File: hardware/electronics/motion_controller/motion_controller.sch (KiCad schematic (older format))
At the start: 186 parts, among them K1 CONN_3, K10 CONN_3, K11 CONN_3, K12 CONN_3, K13 CONN_3, K14 CONN_3, K15 CONN_3, K2 CONN_3, K3 CONN_3, K4 CONN_3, K5 CONN_3, K6 CONN_3, K7 CONN_3, K8 CONN_3, K9 CONN_3, P1 CONN_2, P10 CONN_4, P11 CONN_4, P12 CONN_4, P13 CONN_2, P14 CONN_2, P15 CONN_2, P16 CONN_2, P17 CONN_2, P18 CONN_2, P19 CONN_2X2, P2 CONN_5X2, P20 CONN_2X2, P21 CONN_2, P22 CONN_2, P23 CONN_2, P24 CONN_2, P25 CONN_2, P26 CONN_2X2, P27 CONN_2, P28 CONN_2, P29 CONN_2, P3 CONN_2X2, P30 CONN_1, P31 CONN_1, P32 CONN_1, P33 CONN_1, P4 CONN_2, P5 CONN_34X2, P6 CONN_4, P7 CONN_4, P8 CONN_4, P9 CONN_4, U1 TEENSY3.1, U10 OP07, U11 OP07, U12 OP07, U13 OP07, U14 OP07, U15 OP07, U16 OP07, U17 MEA1D0512SC, U18 PJRC_SD_CARD, U2 NC7WZ04, U3 NC7WZ16, U4 NC7WZ16, U5 SSR_DC_6PIN, U6 MAX6176AASA+, U7 OP07, U8 OP07, U9 OP07

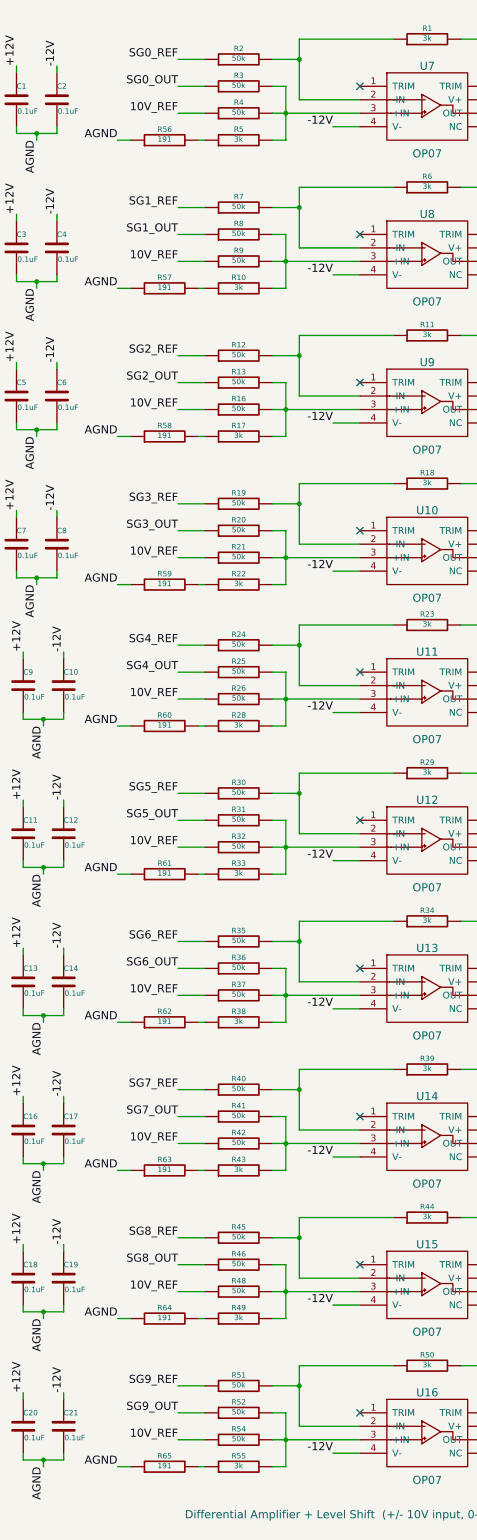
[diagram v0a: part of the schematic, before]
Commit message: Worked on BOM for motion controller PCB.
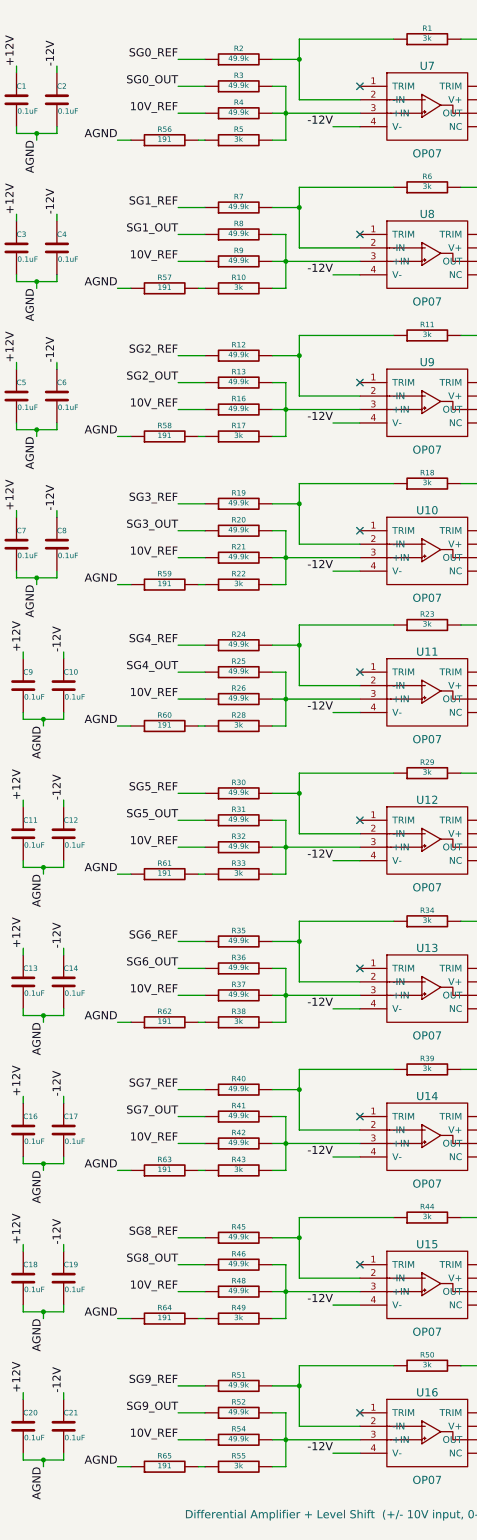
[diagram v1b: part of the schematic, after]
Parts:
- R12, R13, R16, R19, R2, R20, R21, R24, R25, R26, R3, R30, R31, R32, R35, R36, R37, R4, R40, R41, R42, R45, R46, R48, R51, R52, R54, R7, R8, R9: value 50k -> 49.9k
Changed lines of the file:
@@
 Sheet 1 1
 Title ""
-Date "11 apr 2016"
+Date "14 apr 2016"
 Rev ""
 Comp ""
@@
 P 12450 1250
 F 0 "R3" V 12530 1250 40  0000 C CNN
-F 1 "50k" V 12457 1251 40  0000 C CNN
+F 1 "49.9k" V 12457 1251 40  0000 C CNN
 F 2 "~" V 12380 1250 30  0000 C CNN
 F 3 "~" H 12450 1250 30  0000 C CNN
@@
 P 12450 1050
 F 0 "R2" V 12530 1050 40  0000 C CNN
-F 1 "50k" V 12457 1051 40  0000 C CNN
+F 1 "49.9k" V 12457 1051 40  0000 C CNN
 F 2 "~" V 12380 1050 30  0000 C CNN
 F 3 "~" H 12450 1050 30  0000 C CNN
@@
 P 12450 1450
 F 0 "R4" V 12530 1450 40  0000 C CNN
-F 1 "50k" V 12457 1451 40  0000 C CNN
+F 1 "49.9k" V 12457 1451 40  0000 C CNN
 F 2 "~" V 12380 1450 30  0000 C CNN
 F 3 "~" H 12450 1450 30  0000 C CNN
@@
 P 12450 2350
 F 0 "R8" V 12530 2350 40  0000 C CNN
-F 1 "50k" V 12457 2351 40  0000 C CNN
+F 1 "49.9k" V 12457 2351 40  0000 C CNN
 F 2 "~" V 12380 2350 30  0000 C CNN
 F 3 "~" H 12450 2350 30  0000 C CNN
@@
 P 12450 2150
 F 0 "R7" V 12530 2150 40  0000 C CNN
-F 1 "50k" V 12457 2151 40  0000 C CNN
+F 1 "49.9k" V 12457 2151 40  0000 C CNN
 F 2 "~" V 12380 2150 30  0000 C CNN
 F 3 "~" H 12450 2150 30  0000 C CNN
@@
 P 12450 2550
 F 0 "R9" V 12530 2550 40  0000 C CNN
-F 1 "50k" V 12457 2551 40  0000 C CNN
+F 1 "49.9k" V 12457 2551 40  0000 C CNN
 F 2 "~" V 12380 2550 30  0000 C CNN
 F 3 "~" H 12450 2550 30  0000 C CNN
@@
 P 12450 3450
 F 0 "R13" V 12530 3450 40  0000 C CNN
-F 1 "50k" V 12457 3451 40  0000 C CNN
+F 1 "49.9k" V 12457 3451 40  0000 C CNN
 F 2 "~" V 12380 3450 30  0000 C CNN
 F 3 "~" H 12450 3450 30  0000 C CNN
@@
 P 12450 3250
 F 0 "R12" V 12530 3250 40  0000 C CNN
-F 1 "50k" V 12457 3251 40  0000 C CNN
+F 1 "49.9k" V 12457 3251 40  0000 C CNN
 F 2 "~" V 12380 3250 30  0000 C CNN
 F 3 "~" H 12450 3250 30  0000 C CNN
@@
 P 12450 3650
 F 0 "R16" V 12530 3650 40  0000 C CNN
-F 1 "50k" V 12457 3651 40  0000 C CNN
+F 1 "49.9k" V 12457 3651 40  0000 C CNN
 F 2 "~" V 12380 3650 30  0000 C CNN
 F 3 "~" H 12450 3650 30  0000 C CNN
@@
 P 12450 4550
 F 0 "R20" V 12530 4550 40  0000 C CNN
-F 1 "50k" V 12457 4551 40  0000 C CNN
+F 1 "49.9k" V 12457 4551 40  0000 C CNN
 F 2 "~" V 12380 4550 30  0000 C CNN
 F 3 "~" H 12450 4550 30  0000 C CNN
@@
 P 12450 4350
 F 0 "R19" V 12530 4350 40  0000 C CNN
-F 1 "50k" V 12457 4351 40  0000 C CNN
+F 1 "49.9k" V 12457 4351 40  0000 C CNN
 F 2 "~" V 12380 4350 30  0000 C CNN
 F 3 "~" H 12450 4350 30  0000 C CNN
@@
 P 12450 4750
 F 0 "R21" V 12530 4750 40  0000 C CNN
-F 1 "50k" V 12457 4751 40  0000 C CNN
+F 1 "49.9k" V 12457 4751 40  0000 C CNN
 F 2 "~" V 12380 4750 30  0000 C CNN
 F 3 "~" H 12450 4750 30  0000 C CNN
@@
 P 12450 5600
 F 0 "R25" V 12530 5600 40  0000 C CNN
-F 1 "50k" V 12457 5601 40  0000 C CNN
+F 1 "49.9k" V 12457 5601 40  0000 C CNN
 F 2 "~" V 12380 5600 30  0000 C CNN
 F 3 "~" H 12450 5600 30  0000 C CNN
@@
 P 12450 5400
 F 0 "R24" V 12530 5400 40  0000 C CNN
-F 1 "50k" V 12457 5401 40  0000 C CNN
+F 1 "49.9k" V 12457 5401 40  0000 C CNN
 F 2 "~" V 12380 5400 30  0000 C CNN
 F 3 "~" H 12450 5400 30  0000 C CNN
@@
 P 12450 5800
 F 0 "R26" V 12530 5800 40  0000 C CNN
-F 1 "50k" V 12457 5801 40  0000 C CNN
+F 1 "49.9k" V 12457 5801 40  0000 C CNN
 F 2 "~" V 12380 5800 30  0000 C CNN
 F 3 "~" H 12450 5800 30  0000 C CNN
@@
 P 12450 6700
 F 0 "R31" V 12530 6700 40  0000 C CNN
-F 1 "50k" V 12457 6701 40  0000 C CNN
+F 1 "49.9k" V 12457 6701 40  0000 C CNN
 F 2 "~" V 12380 6700 30  0000 C CNN
 F 3 "~" H 12450 6700 30  0000 C CNN
@@
 P 12450 6500
 F 0 "R30" V 12530 6500 40  0000 C CNN
-F 1 "50k" V 12457 6501 40  0000 C CNN
+F 1 "49.9k" V 12457 6501 40  0000 C CNN
 F 2 "~" V 12380 6500 30  0000 C CNN
 F 3 "~" H 12450 6500 30  0000 C CNN
@@
 P 12450 6900
 F 0 "R32" V 12530 6900 40  0000 C CNN
-F 1 "50k" V 12457 6901 40  0000 C CNN
+F 1 "49.9k" V 12457 6901 40  0000 C CNN
 F 2 "~" V 12380 6900 30  0000 C CNN
 F 3 "~" H 12450 6900 30  0000 C CNN
@@
 P 12450 7800
 F 0 "R36" V 12530 7800 40  0000 C CNN
-F 1 "50k" V 12457 7801 40  0000 C CNN
+F 1 "49.9k" V 12457 7801 40  0000 C CNN
 F 2 "~" V 12380 7800 30  0000 C CNN
 F 3 "~" H 12450 7800 30  0000 C CNN
@@
 P 12450 7600
 F 0 "R35" V 12530 7600 40  0000 C CNN
-F 1 "50k" V 12457 7601 40  0000 C CNN
+F 1 "49.9k" V 12457 7601 40  0000 C CNN
 F 2 "~" V 12380 7600 30  0000 C CNN
 F 3 "~" H 12450 7600 30  0000 C CNN
@@
 P 12450 8000
 F 0 "R37" V 12530 8000 40  0000 C CNN
-F 1 "50k" V 12457 8001 40  0000 C CNN
+F 1 "49.9k" V 12457 8001 40  0000 C CNN
 F 2 "~" V 12380 8000 30  0000 C CNN
 F 3 "~" H 12450 8000 30  0000 C CNN
@@
 P 12450 8900
 F 0 "R41" V 12530 8900 40  0000 C CNN
-F 1 "50k" V 12457 8901 40  0000 C CNN
+F 1 "49.9k" V 12457 8901 40  0000 C CNN
 F 2 "~" V 12380 8900 30  0000 C CNN
 F 3 "~" H 12450 8900 30  0000 C CNN
@@
 P 12450 8700
 F 0 "R40" V 12530 8700 40  0000 C CNN
-F 1 "50k" V 12457 8701 40  0000 C CNN
+F 1 "49.9k" V 12457 8701 40  0000 C CNN
 F 2 "~" V 12380 8700 30  0000 C CNN
 F 3 "~" H 12450 8700 30  0000 C CNN
@@
 P 12450 9100
 F 0 "R42" V 12530 9100 40  0000 C CNN
-F 1 "50k" V 12457 9101 40  0000 C CNN
+F 1 "49.9k" V 12457 9101 40  0000 C CNN
 F 2 "~" V 12380 9100 30  0000 C CNN
 F 3 "~" H 12450 9100 30  0000 C CNN
@@
 P 12450 10000
 F 0 "R46" V 12530 10000 40  0000 C CNN
-F 1 "50k" V 12457 10001 40  0000 C CNN
+F 1 "49.9k" V 12457 10001 40  0000 C CNN
 F 2 "~" V 12380 10000 30  0000 C CNN
 F 3 "~" H 12450 10000 30  0000 C CNN
@@
 P 12450 9800
 F 0 "R45" V 12530 9800 40  0000 C CNN
-F 1 "50k" V 12457 9801 40  0000 C CNN
+F 1 "49.9k" V 12457 9801 40  0000 C CNN
 F 2 "~" V 12380 9800 30  0000 C CNN
 F 3 "~" H 12450 9800 30  0000 C CNN
@@
 P 12450 10200
 F 0 "R48" V 12530 10200 40  0000 C CNN
-F 1 "50k" V 12457 10201 40  0000 C CNN
+F 1 "49.9k" V 12457 10201 40  0000 C CNN
 F 2 "~" V 12380 10200 30  0000 C CNN
 F 3 "~" H 12450 10200 30  0000 C CNN
@@
 P 12450 11100
 F 0 "R52" V 12530 11100 40  0000 C CNN
-F 1 "50k" V 12457 11101 40  0000 C CNN
+F 1 "49.9k" V 12457 11101 40  0000 C CNN
 F 2 "~" V 12380 11100 30  0000 C CNN
 F 3 "~" H 12450 11100 30  0000 C CNN
@@
 P 12450 10900
 F 0 "R51" V 12530 10900 40  0000 C CNN
-F 1 "50k" V 12457 10901 40  0000 C CNN
+F 1 "49.9k" V 12457 10901 40  0000 C CNN
 F 2 "~" V 12380 10900 30  0000 C CNN
 F 3 "~" H 12450 10900 30  0000 C CNN
@@
 P 12450 11300
 F 0 "R54" V 12530 11300 40  0000 C CNN
-F 1 "50k" V 12457 11301 40  0000 C CNN
+F 1 "49.9k" V 12457 11301 40  0000 C CNN
 F 2 "~" V 12380 11300 30  0000 C CNN
 F 3 "~" H 12450 11300 30  0000 C CNN

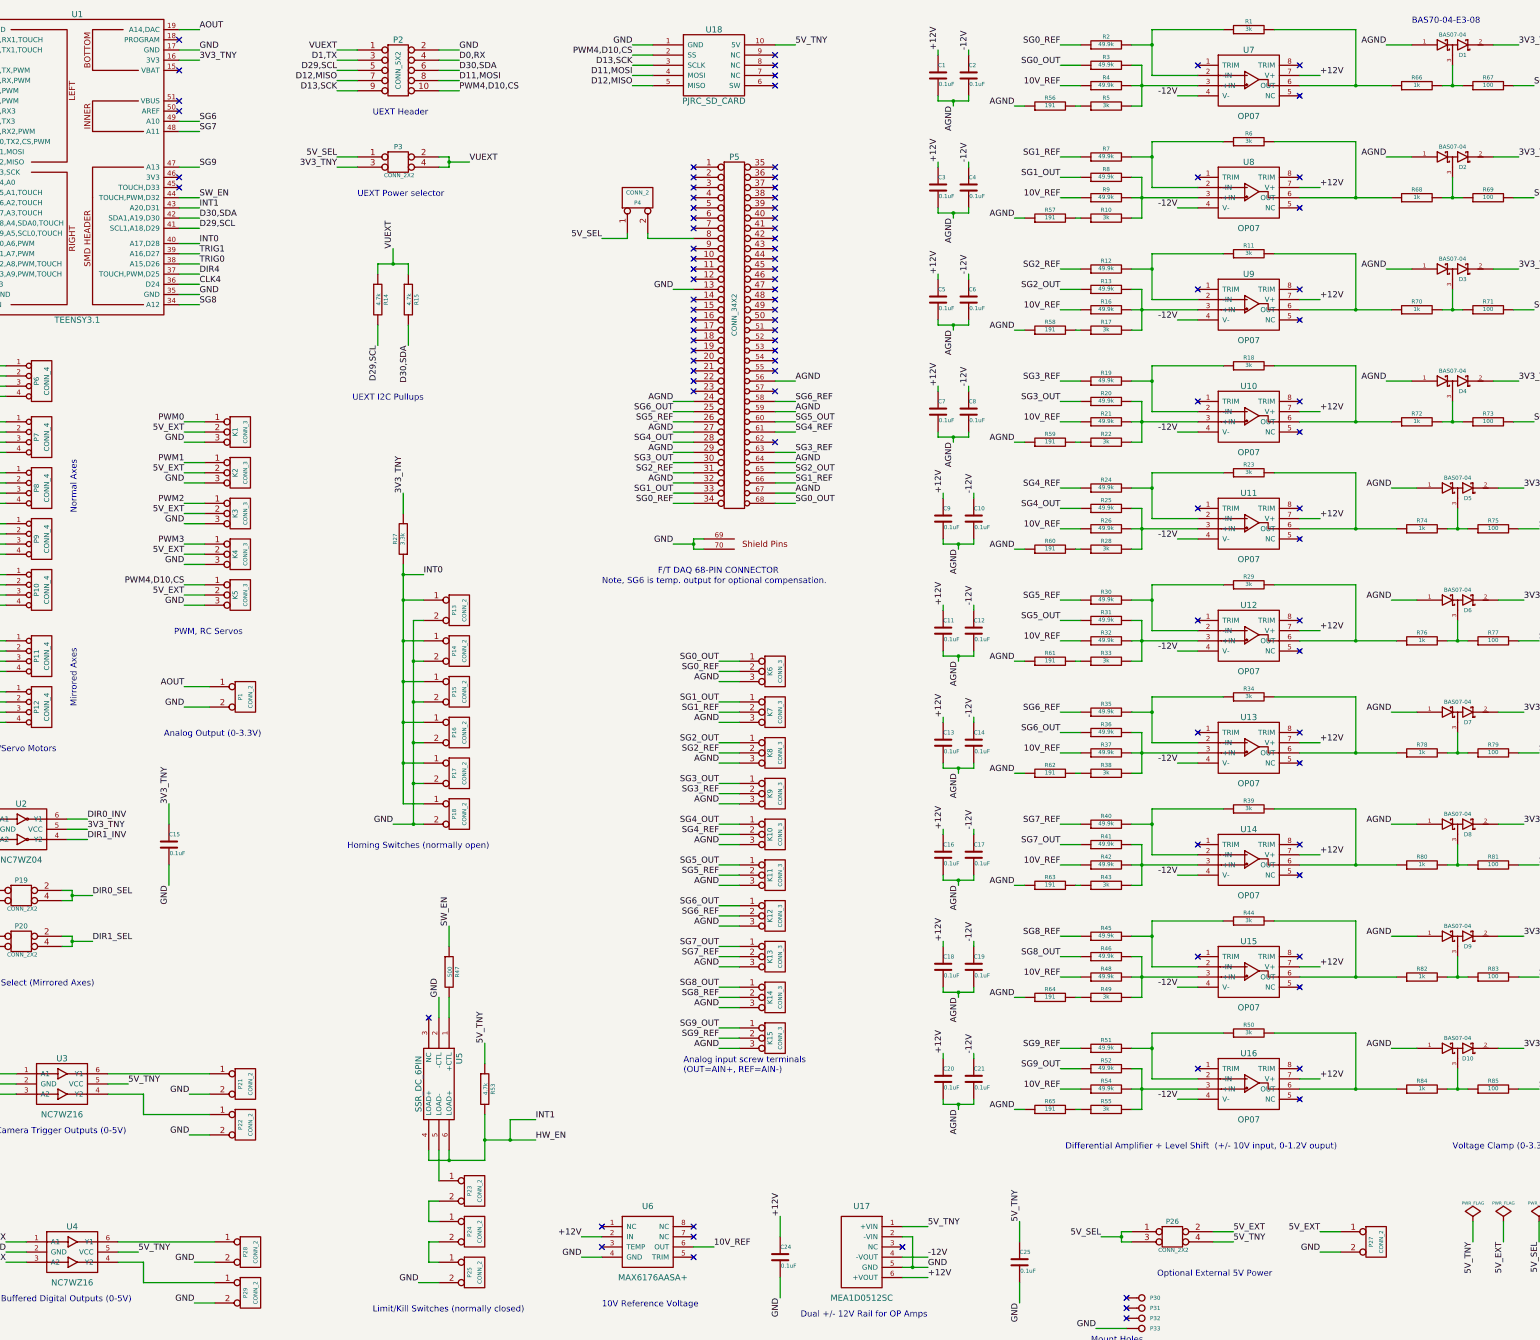
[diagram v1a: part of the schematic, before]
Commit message: Added sympy derivation of differential amplifier gain for motion controller pcb.
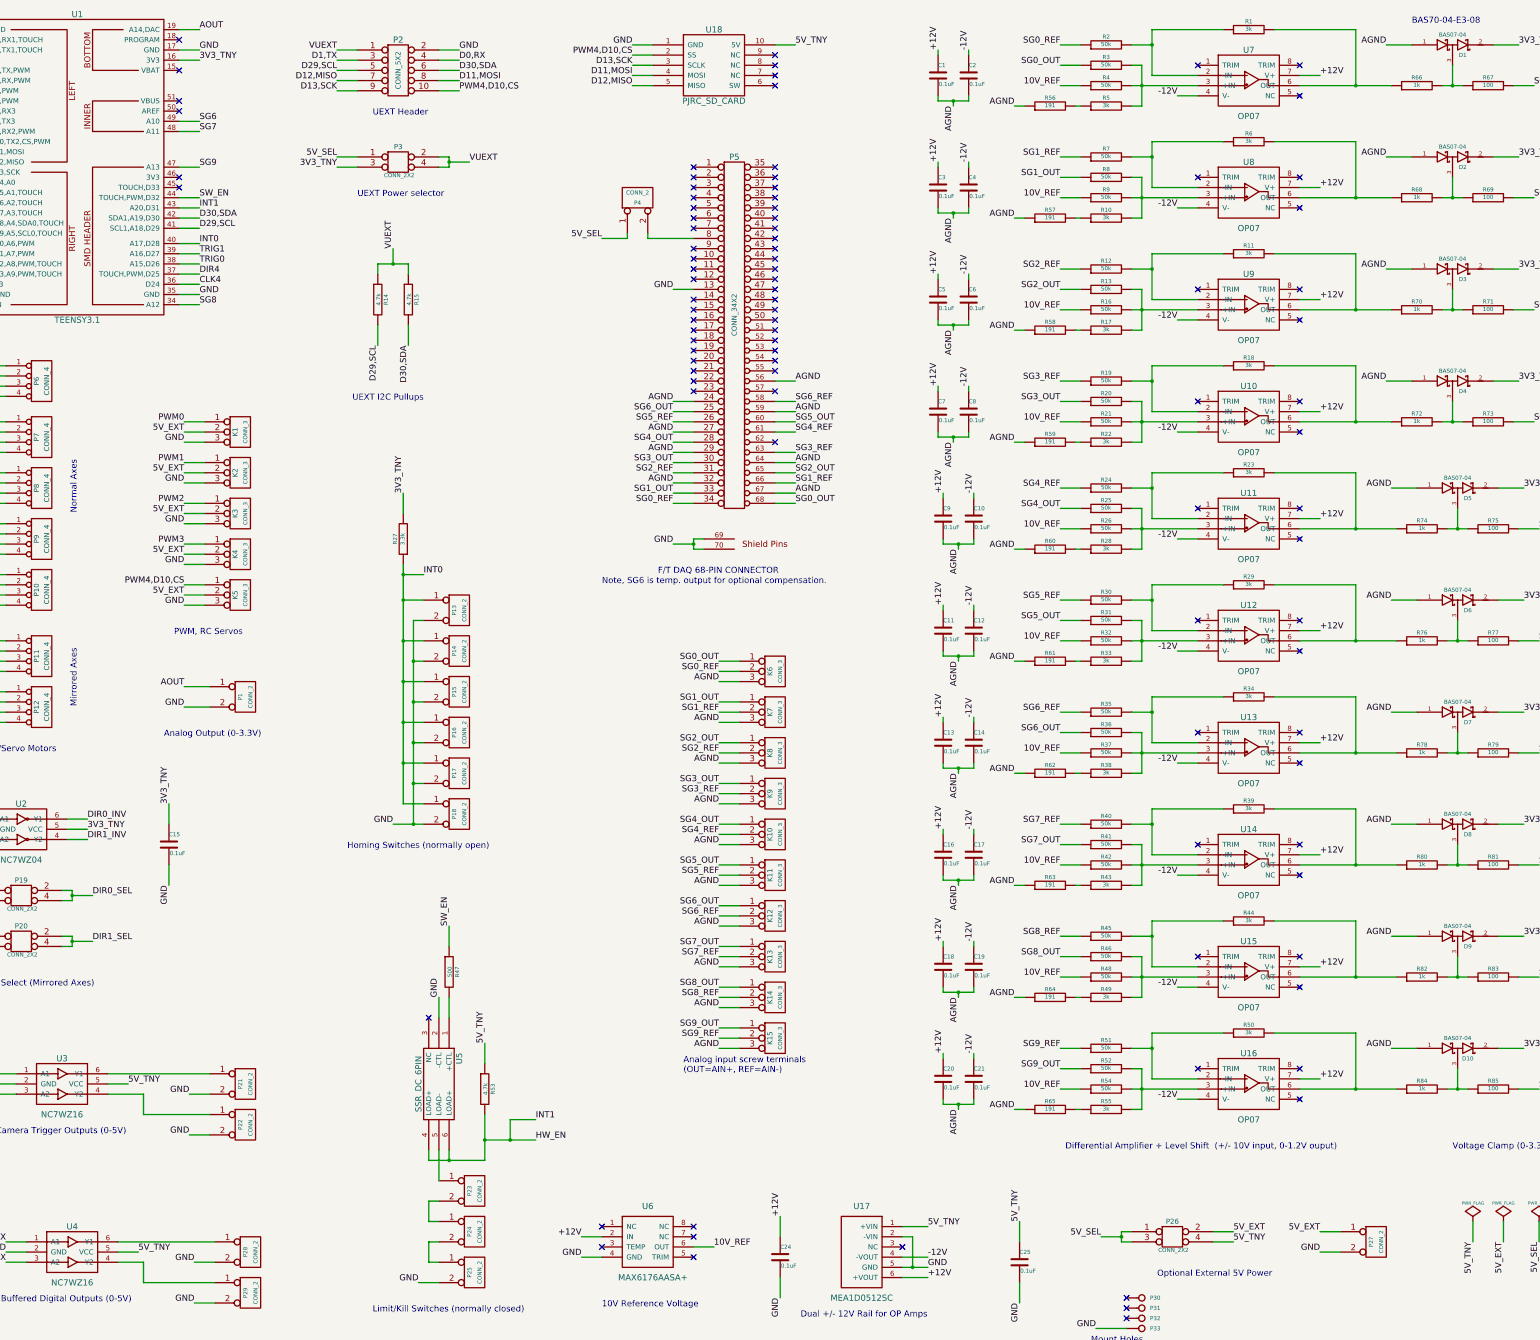
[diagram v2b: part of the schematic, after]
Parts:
- R12, R13, R16, R19, R2, R20, R21, R24, R25, R26, R3, R30, R31, R32, R35, R36, R37, R4, R40, R41, R42, R45, R46, R48, R51, R52, R54, R7, R8, R9: value 49.9k -> 50k
